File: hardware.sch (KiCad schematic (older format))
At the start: 2 parts

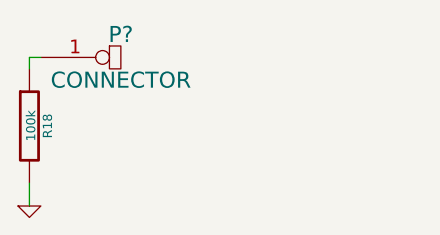
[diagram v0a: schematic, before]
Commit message: Finishing bom integration with schematic.
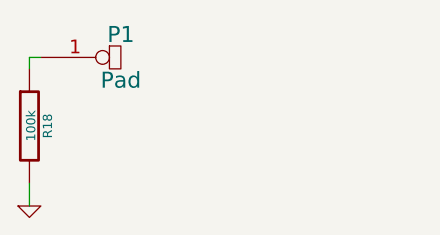
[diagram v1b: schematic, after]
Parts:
- P1: renamed from P?; value CONNECTOR -> Pad
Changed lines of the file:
@@
 LIBS:p_samtec
 LIBS:w_transistor
+LIBS:w_analog
 LIBS:distro-cache
 EELAYER 27 0
@@
 Sheet 9 9
 Title ""
-Date "21 aug 2015"
+Date "22 aug 2015"
 Rev ""
 Comp ""
@@
 $EndDescr
 $Comp
-L CONNECTOR P?
+L CONNECTOR P1
 U 1 1 55D6D1EC
 P 4250 3800
-F 0 "P?" H 4600 3900 70  0000 C CNN
-F 1 "CONNECTOR" H 4600 3700 70  0000 C CNN
+F 0 "P1" H 4600 3900 70  0000 C CNN
+F 1 "Pad" H 4600 3700 70  0000 C CNN
 F 2 "~" H 4250 3800 60  0000 C CNN
 F 3 "~" H 4250 3800 60  0000 C CNN

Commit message: Updating design with new 12v bus.
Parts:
- R18: Digikey P100KACT-ND -> P100KCCT-ND
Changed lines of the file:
@@
 LIBS:w_transistor
 LIBS:w_analog
+LIBS:p_meas_spec
 LIBS:distro-cache
 EELAYER 27 0
@@
 F 2 "~" V 4130 4100 30  0000 C CNN
 F 3 "~" H 4200 4100 30  0000 C CNN
-F 4 "P100KACT-ND" V 4200 4100 60  0001 C CNN "Digikey"
+F 4 "P100KCCT-ND" V 4200 4100 60  0001 C CNN "Digikey"
 	1    4200 4100
 	1    0    0    -1
 $EndComp
 $Comp
-L GND #PWR0143
+L GND #PWR0170
 U 1 1 55D6D20A
 P 4200 4450
-F 0 "#PWR0143" H 4200 4450 30  0001 C CNN
+F 0 "#PWR0170" H 4200 4450 30  0001 C CNN
 F 1 "GND" H 4200 4380 30  0001 C CNN
 F 2 "" H 4200 4450 60  0000 C CNN

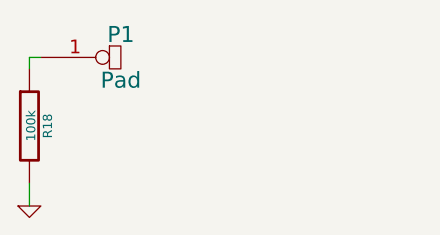
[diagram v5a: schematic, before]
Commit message: Updating layout and component pad configs.
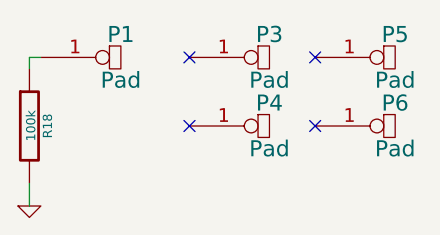
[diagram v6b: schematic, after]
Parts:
- added P3, P4, P5, P6: Pad, ~, symbol CONNECTOR
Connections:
- no-connect marks 0 -> 4
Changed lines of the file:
@@
 Sheet 9 9
 Title ""
-Date "24 aug 2015"
+Date "25 aug 2015"
 Rev ""
 Comp ""
@@
 Wire Wire Line
 	4200 3800 4250 3800
+$Comp
+L CONNECTOR P3
+U 1 1 55DCC507
+P 4900 3800
+F 0 "P3" H 5250 3900 70  0000 C CNN
+F 1 "Pad" H 5250 3700 70  0000 C CNN
+F 2 "~" H 4900 3800 60  0000 C CNN
+F 3 "~" H 4900 3800 60  0000 C CNN
+	1    4900 3800
+	1    0    0    -1
+$EndComp
+$Comp
+L CONNECTOR P5
+U 1 1 55DCC50D
+P 5450 3800
+F 0 "P5" H 5800 3900 70  0000 C CNN
+F 1 "Pad" H 5800 3700 70  0000 C CNN
+F 2 "~" H 5450 3800 60  0000 C CNN
+F 3 "~" H 5450 3800 60  0000 C CNN
+	1    5450 3800
+	1    0    0    -1
+$EndComp
+$Comp
+L CONNECTOR P4
+U 1 1 55DCC519
+P 4900 4100
+F 0 "P4" H 5250 4200 70  0000 C CNN
+F 1 "Pad" H 5250 4000 70  0000 C CNN
+F 2 "~" H 4900 4100 60  0000 C CNN
+F 3 "~" H 4900 4100 60  0000 C CNN
+	1    4900 4100
+	1    0    0    -1
+$EndComp
+$Comp
+L CONNECTOR P6
+U 1 1 55DCC51F
+P 5450 4100
+F 0 "P6" H 5800 4200 70  0000 C CNN
+F 1 "Pad" H 5800 4000 70  0000 C CNN
+F 2 "~" H 5450 4100 60  0000 C CNN
+F 3 "~" H 5450 4100 60  0000 C CNN
+	1    5450 4100
+	1    0    0    -1
+$EndComp
+NoConn ~ 5450 4100
+NoConn ~ 5450 3800
+NoConn ~ 4900 3800
+NoConn ~ 4900 4100
 $EndSCHEMATC
